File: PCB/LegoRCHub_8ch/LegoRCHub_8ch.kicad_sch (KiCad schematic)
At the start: 35 parts, among them J1 Conn_01x02, J2 Conn_01x02, J3 Conn_01x02, J4 Conn_01x02, J5 Conn_01x02, J6 Conn_01x03, J7 Conn_01x03, J8 Conn_01x03, J9 Conn_01x02, U1 DRV8872DDA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

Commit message: LegoRCHub_8ch: working on pcb design...
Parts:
- J9: footprint (none) -> Connector_AMASS:AMASS_XT30U-M_1x02_P5.0mm_Vertical
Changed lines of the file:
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@@
       (effects (font (size 1.27 1.27)) (justify left))
     )
-    (property "Footprint" "" (id 2) (at 115.316 135.636 0)
+    (property "Footprint" "Connector_AMASS:AMASS_XT30U-M_1x02_P5.0mm_Vertical" (id 2) (at 115.316 135.636 0)
       (effects (font (size 1.27 1.27)) hide)
     )
@@
     )
     (path "/b91526a1-4a34-4124-9d96-fa092757f2e9"
-      (reference "J9") (unit 1) (value "Conn_01x02") (footprint "")
+      (reference "J9") (unit 1) (value "Conn_01x02") (footprint "Connector_AMASS:AMASS_XT30U-M_1x02_P5.0mm_Vertical")
     )
     (path "/69d15c88-8105-4706-b7b5-8a3efcccbddc"

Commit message: LegoRCHub_8ch: working on pcb design...
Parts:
- removed U7: ATtiny1607-M, Package_DFN_QFN:QFN-24-1EP_4x4mm_P0.5mm_EP2.6x2.6mm, symbol MCU_Microchip_ATtiny:ATtiny1607-M
- added U7: ATtiny3226-X, Package_SO:SSOP-20_5.3x7.2mm_P0.65mm, symbol MCU_Microchip_ATtiny:ATtiny3226-X
- C13: footprint Capacitor_SMD:C_1206_3216Metric_Pad1.33x1.80mm_HandSolder -> Capacitor_SMD:C_0603_1608Metric_Pad1.08x0.95mm_HandSolder
- J1, J2, J3, J4, J5: footprint Connector_PinHeader_2.54mm:PinHeader_1x02_P2.54mm_Vertical -> Connector_PinHeader_2.54mm:PinHeader_1x02_P2.54mm_Vertical_SMD_Pin1Left
- J6, J7, J8: footprint Connector_PinHeader_2.54mm:PinHeader_1x03_P2.54mm_Vertical -> Connector_PinHeader_2.54mm:PinHeader_1x03_P2.54mm_Vertical_SMD_Pin1Left
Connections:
- net +BATT: no longer C13.2, C14.2
- net CH1_2: now also U7.18 (PA2)
- net CH1_3: now also U7.17 (PA1)
- net CH2_2: now also U7.13 (PC1)
- net CH2_3: now also U7.12 (PC0)
- net CH3_2: now also U7.15 (PC3)
- net CH3_3: now also U7.14 (PC2)
- net CH4_2: now also U7.19 (PA3)
- net CH4_3: now also U7.2 (PA4)
- net CH5_2: now also U7.3 (PA5)
- net CH5_3: now also U7.4 (PA6)
- net CH6_3: now also U7.9 (PB2)
- net CH7_3: now also U7.10 (PB1)
- net CH8_3: now also U7.11 (PB0)
- net GND: now also U7.20 (GND)
- net VCC: now also C13.2, C14.2, U7.1 (VCC)
- no-connect marks 9 -> 5
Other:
- moved on the sheet: C14

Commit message: LegoRCHub_8ch: finished PCB (beta 1)
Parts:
- added J10: Conn_01x02, Connector_PinHeader_2.54mm:PinHeader_1x02_P2.54mm_Vertical, symbol Connector_Generic:Conn_01x02
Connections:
- net CH1_2: now also U7.7 (PB4); no longer U7.18 (PA2)
- net CH1_3: now also U7.6 (PB5); no longer U7.17 (PA1)
- net CH2_2: now also U7.5 (PA7); no longer U7.13 (PC1)
- net CH2_3: now also U7.4 (PA6); no longer U7.12 (PC0)
- net CH3_2: now also U7.3 (PA5); no longer U7.15 (PC3)
- net CH3_3: now also U7.2 (PA4); no longer U7.14 (PC2)
- net CH4_2: now also U7.14 (PC2); no longer U7.19 (PA3)
- net CH4_3: now also U7.15 (PC3); no longer U7.2 (PA4)
- net CH5_2: now also U7.17 (PA1); no longer U7.3 (PA5)
- net CH5_3: now also U7.18 (PA2); no longer U7.4 (PA6)
- net CH6_3: now also U7.10 (PB1); no longer U7.9 (PB2)
- net CH7_3: now also U7.12 (PC0); no longer U7.10 (PB1)
- net CH8_3: now also U7.19 (PA3); no longer U7.11 (PB0)
- net GND: now also J10.1 (Pin_1)
- net UPDI: now reaches U7.16 (~{RESET}/PA0)
- net UPDI: now also J10.2 (Pin_2)
- no-connect marks 5 -> 0
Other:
- moved on the sheet: C13, C14, U7

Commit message: LegoRCHub_8ch: finished PCB (beta 2)
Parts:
- added C15: 470uF, Capacitor_SMD:CP_Elec_8x10.5, symbol Device:C_Polarized_Small
- U6: footprint Package_TO_SOT_SMD:SOT-223-3_TabPin2 -> Package_TO_SOT_SMD:SOT-89-3_Handsoldering
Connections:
- net +BATT: now also C15.1
- net CH4_2: now also U7.15 (PC3); no longer U7.14 (PC2)
- net CH4_3: now also U7.14 (PC2); no longer U7.15 (PC3)
- net CH5_2: now also U7.18 (PA2); no longer U7.17 (PA1)
- net CH5_3: now also U7.17 (PA1); no longer U7.18 (PA2)
- net CH8_3: now also U7.11 (PB0); no longer U7.19 (PA3)
- net GND: now also C15.2
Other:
- moved on the sheet: J9

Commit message: LegoRCHub_8ch: finished PCB (beta 4)
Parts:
- removed C13: 10uF, Capacitor_SMD:C_0603_1608Metric_Pad1.08x0.95mm_HandSolder, symbol Device:C_Small
- removed R1, R2, R3, R4, R5: 10k, Resistor_SMD:R_0603_1608Metric_Pad0.98x0.95mm_HandSolder, symbol Device:R_Small
- added C16: 470uF, Capacitor_SMD:CP_Elec_8x10.5, symbol Device:C_Polarized_Small
- added J11: Conn_01x03, Connector_JST:JST_XH_B3B-XH-A_1x03_P2.50mm_Vertical, symbol Connector_Generic:Conn_01x03
- J1, J2, J3, J4, J5: footprint Connector_PinHeader_2.54mm:PinHeader_1x02_P2.54mm_Vertical_SMD_Pin1Left -> Connector_PinHeader_2.54mm:PinHeader_1x02_P2.54mm_Vertical
- J10: footprint Connector_PinHeader_2.54mm:PinHeader_1x02_P2.54mm_Vertical -> Connector_PinSocket_2.54mm:PinSocket_1x02_P2.54mm_Vertical
- J6, J7, J8: footprint Connector_PinHeader_2.54mm:PinHeader_1x03_P2.54mm_Vertical_SMD_Pin1Left -> Connector_PinHeader_2.54mm:PinHeader_1x03_P2.54mm_Vertical
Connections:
- net +BATT: now also C16.1
- net CH1_2: now also U7.18 (PA2); no longer U7.7 (PB4)
- net CH1_3: now also U7.19 (PA3); no longer U7.6 (PB5)
- net CH2_2: now also U7.15 (PC3); no longer U7.5 (PA7)
- net CH2_3: now also U7.17 (PA1); no longer U7.4 (PA6)
- net CH3_2: now also U7.13 (PC1); no longer U7.3 (PA5)
- net CH3_3: now also U7.14 (PC2); no longer U7.2 (PA4)
- net CH4_2: now also U7.3 (PA5); no longer U7.15 (PC3)
- net CH4_3: now also U7.2 (PA4); no longer U7.14 (PC2)
- net CH5_2: now also U7.9 (PB2); no longer U7.18 (PA2)
- net CH5_3: now also U7.10 (PB1); no longer U7.17 (PA1)
- net GND: now also C16.2, J11.3 (Pin_3)
- net VCC: now also J11.2 (Pin_2)
- net IBus: now reaches U7.8 (PB3)
- net IBus: now also J11.1 (Pin_1)
- net CH6_3 renamed CH6
- net CH6: now also U7.4 (PA6); no longer U7.10 (PB1)
- net CH7_3: no longer names the net of U7.12 (PC0)
- net CH7_3: no longer J7.3 (Pin_3)
- net CH8_3: no longer names the net of U7.11 (PB0)
- net CH8_3: no longer J8.3 (Pin_3)
- new net CH7: J7.3 (Pin_3), U7.5 (PA7)
- new net CH8: J8.3 (Pin_3), U7.6 (PB5)

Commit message: LegoRCHub_8ch: finished PCB (beta 5)
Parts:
- removed C16: 470uF, Capacitor_SMD:CP_Elec_8x10.5, symbol Device:C_Polarized_Small
- added D1: Blue, LED_SMD:LED_0805_2012Metric_Pad1.15x1.40mm_HandSolder, symbol Device:LED_Small
- added R1: 4.7k, Resistor_SMD:R_0805_2012Metric_Pad1.20x1.40mm_HandSolder, symbol Device:R_Small
- C10, C11, C14, C2, C4, C6, C8: footprint Capacitor_SMD:C_0603_1608Metric_Pad1.08x0.95mm_HandSolder -> Capacitor_SMD:C_0805_2012Metric_Pad1.18x1.45mm_HandSolder
- C12: value 22uF -> 47uF; footprint Capacitor_SMD:C_0603_1608Metric_Pad1.08x0.95mm_HandSolder -> Capacitor_SMD:C_0805_2012Metric_Pad1.18x1.45mm_HandSolder
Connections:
- net GND: now also J11.1 (Pin_1); no longer J11.3 (Pin_3)
- net IBus: now also J11.3 (Pin_3); no longer J11.1 (Pin_1)
- net VCC: now also R1.1
- net at U7.11 (PB0): now also D1.2 (A)
- new net: D1.1 (K), R1.2

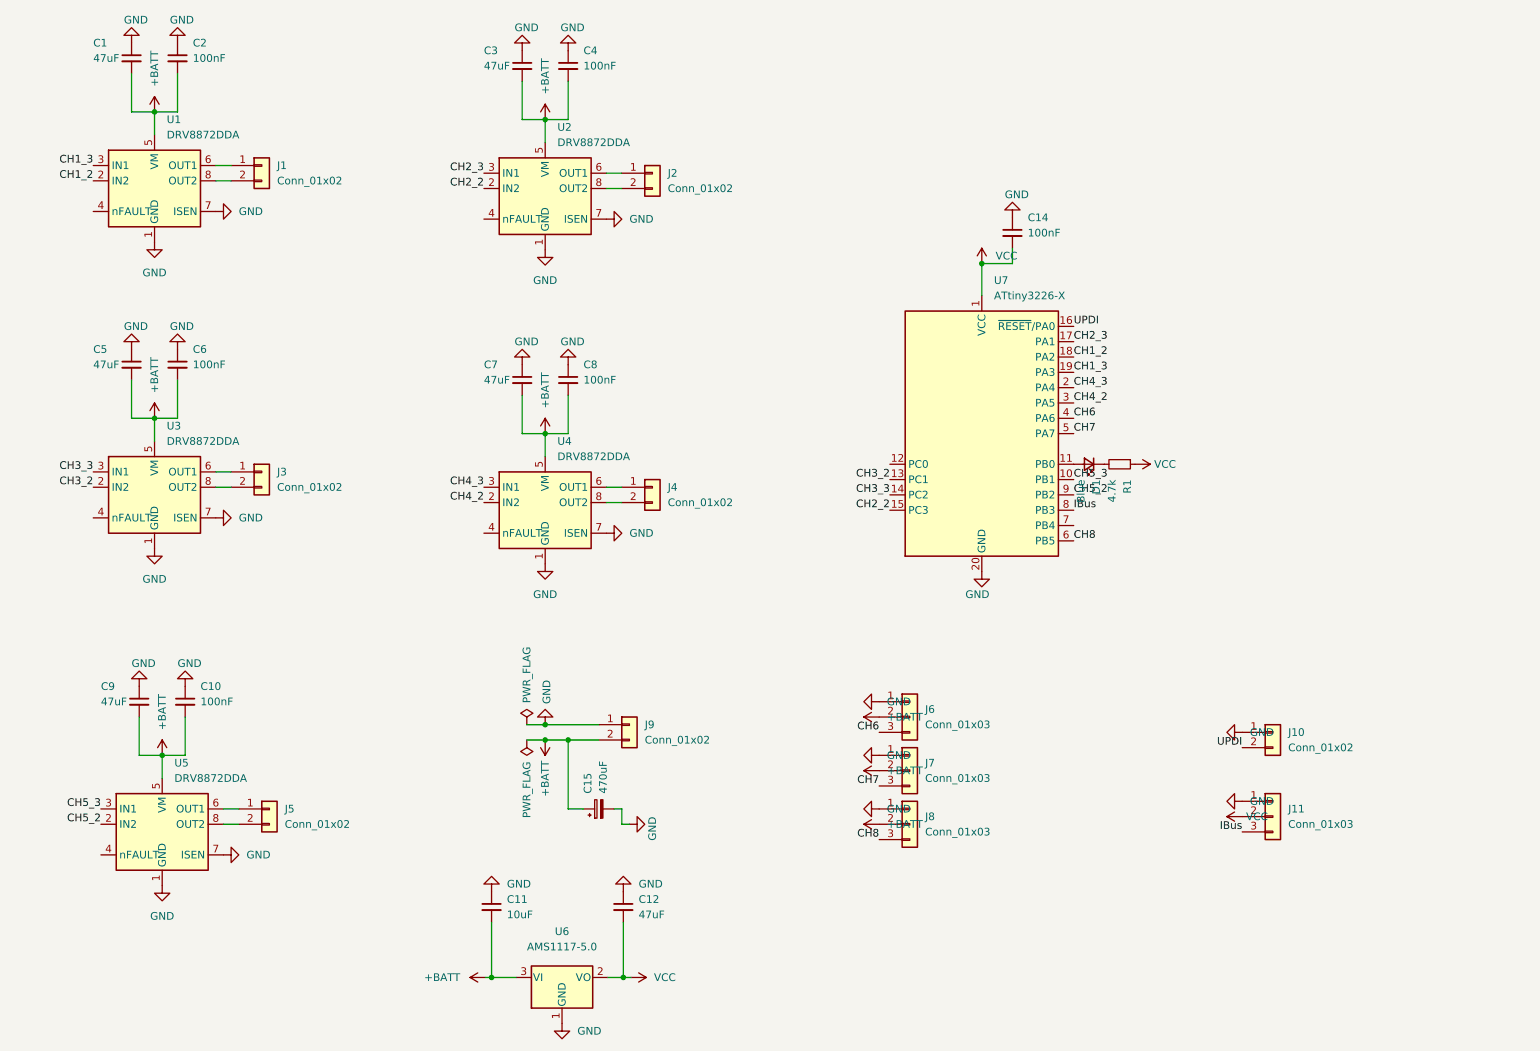
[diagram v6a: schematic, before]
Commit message: LegoRCHub_8ch: beta 6: simplified design with 4/4 layout
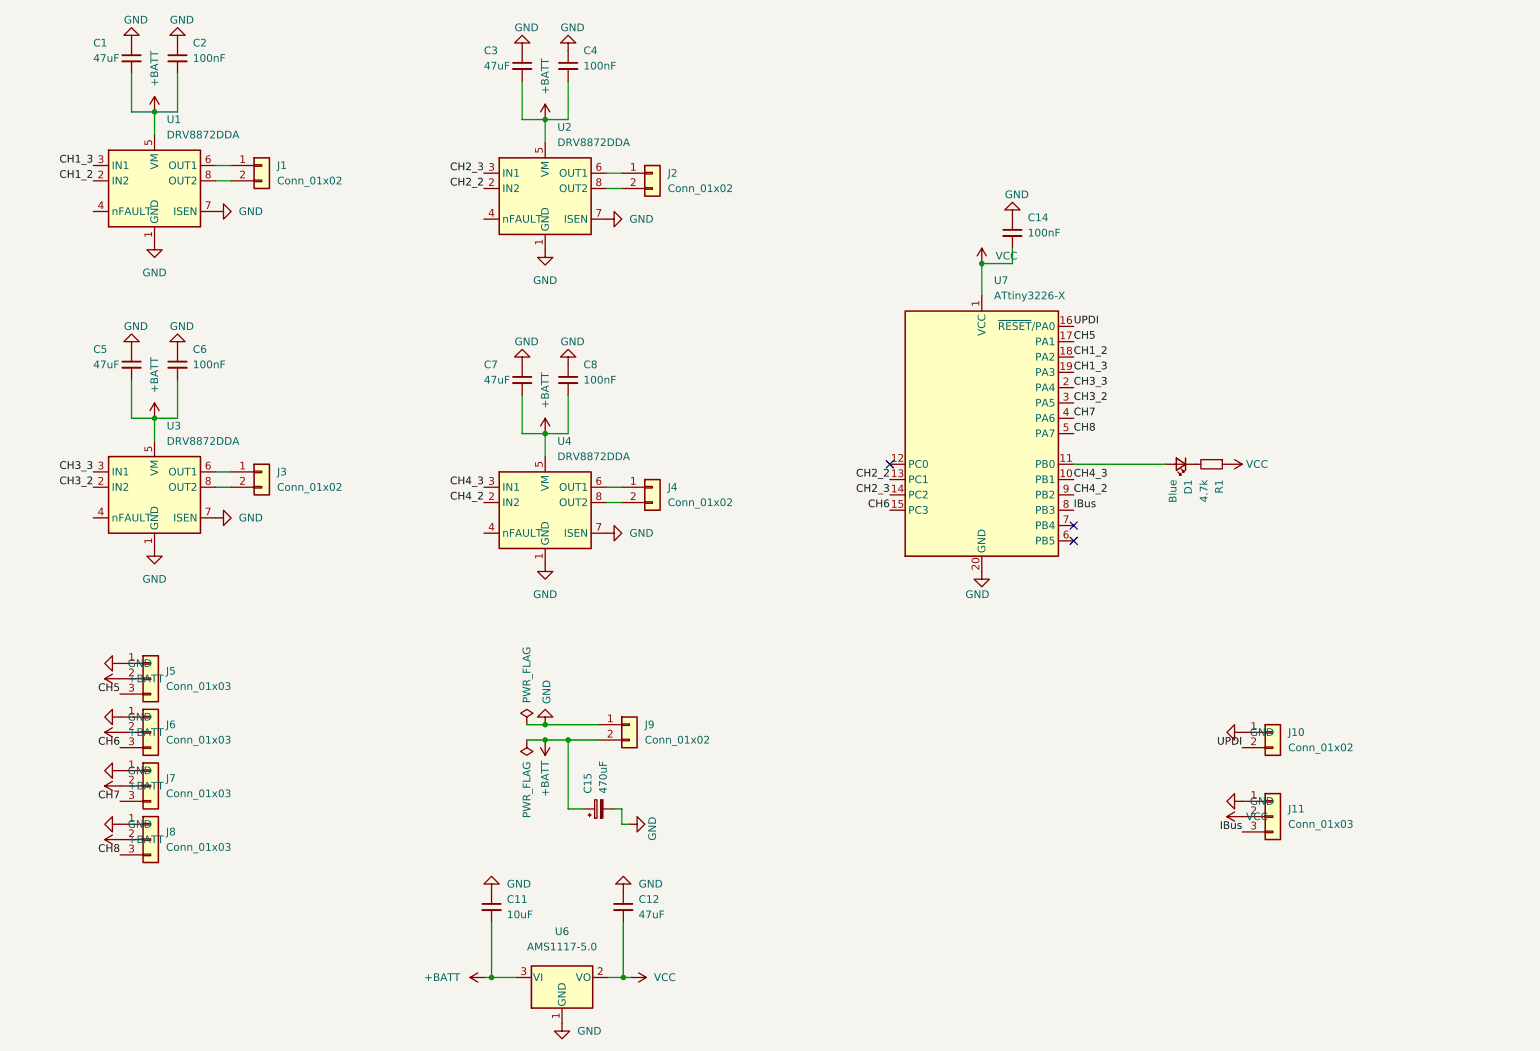
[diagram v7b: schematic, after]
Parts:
- removed C10: 100nF, Capacitor_SMD:C_0805_2012Metric_Pad1.18x1.45mm_HandSolder, symbol Device:C_Small
- removed C9: 47uF, Capacitor_SMD:C_1206_3216Metric_Pad1.33x1.80mm_HandSolder, symbol Device:C_Small
- removed J5: Conn_01x02, Connector_PinHeader_2.54mm:PinHeader_1x02_P2.54mm_Vertical, symbol Connector_Generic:Conn_01x02
- removed U5: DRV8872DDA, Package_SO:Texas_HTSOP-8-1EP_3.9x4.9mm_P1.27mm_EP2.95x4.9mm_Mask2.4x3.1mm_ThermalVias, symbol Driver_Motor:DRV8872DDA
- added J5: Conn_01x03, Connector_PinHeader_2.54mm:PinHeader_1x03_P2.54mm_Vertical, symbol Connector_Generic:Conn_01x03
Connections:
- net CH5_2 is gone; now on net CH4_2: U7.9 (PB2)
- net CH5_3 is gone; now on net CH4_3: U7.10 (PB1)
- net +BATT: now also J5.2 (Pin_2)
- net CH2_2: now also U7.13 (PC1); no longer U7.15 (PC3)
- net CH2_3: now also U7.14 (PC2); no longer U7.17 (PA1)
- net CH3_2: now also U7.3 (PA5); no longer U7.13 (PC1)
- net CH3_3: now also U7.2 (PA4); no longer U7.14 (PC2)
- net CH4_2: no longer U7.3 (PA5)
- net CH4_3: no longer U7.2 (PA4)
- net CH6: now also U7.15 (PC3); no longer U7.4 (PA6)
- net CH7: now also U7.4 (PA6); no longer U7.5 (PA7)
- net CH8: now also U7.5 (PA7); no longer U7.6 (PB5)
- net GND: now also J5.1 (Pin_1)
- new net CH5: J5.3 (Pin_3), U7.17 (PA1)
- no-connect marks 0 -> 3
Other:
- moved on the sheet: D1, J6, J7, J8, R1

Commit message: ...
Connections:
- net LED: now reaches D1.2 (A), U7.11 (PB0)
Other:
- moved on the sheet: C11, C12, C15, D1, J10, J11, J9, R1, U6
